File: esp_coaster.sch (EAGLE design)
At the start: 21 parts, among them IC1 ESP-12E/F, U1 MC34063AP

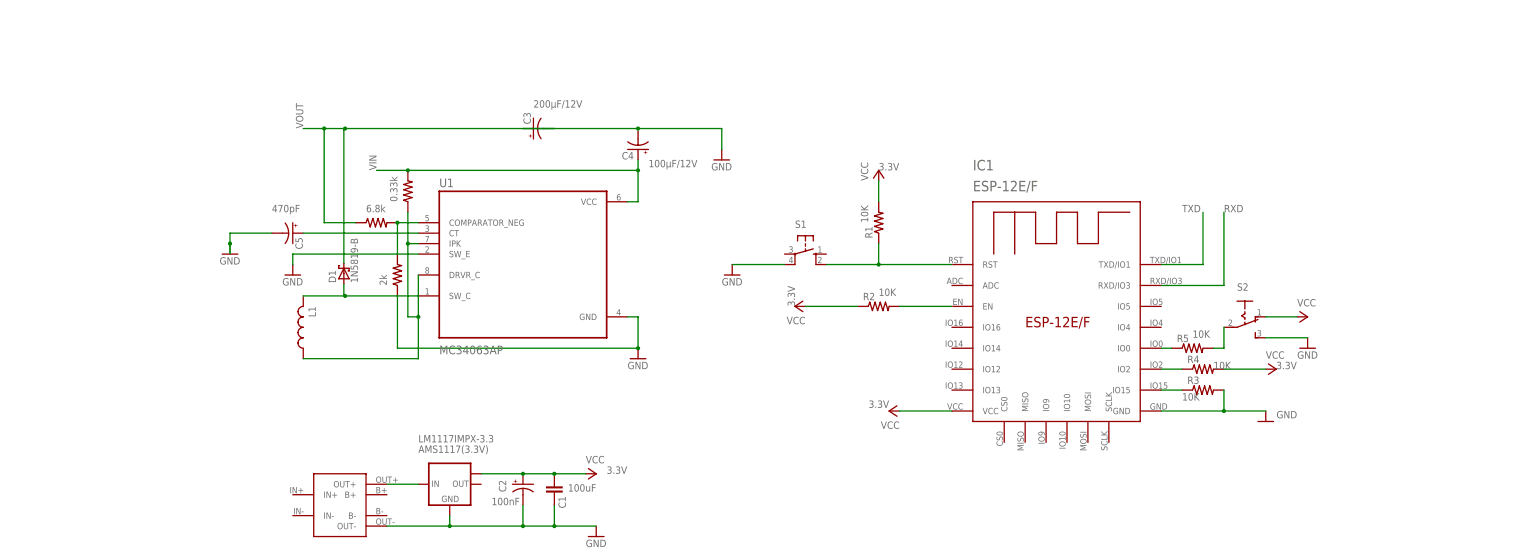
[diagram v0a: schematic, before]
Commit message: add leds
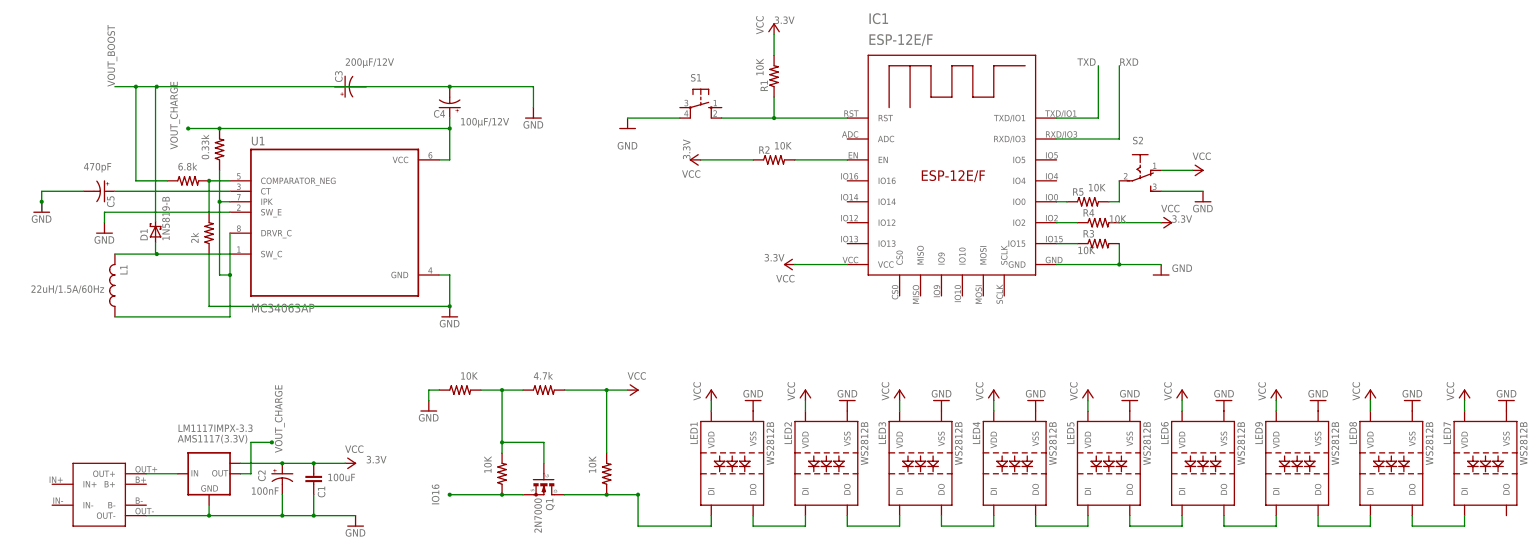
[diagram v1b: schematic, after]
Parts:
- added LED1, LED2, LED3, LED4, LED5, LED6, LED7, LED8, LED9: WS2812B, WS2812:WS2812B
- added Q1: 2N7000, 2N7000:2N7000
- added R10, R11, R12, R9: (no value), rcl:R-US_M2309
- L1: INDUCTOR (none) -> 22uH/1.5A/60Hz
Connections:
- net VOUT renamed VOUT_BOOST
- removed net VIN: C4.+, R8.2, U1.VCC
- new net IO16: Q1.S, R12.1
- new net N$12: LED1.DO, LED2.DI
- new net N$13: LED1.DI, Q1.D, R9.1
- new net N$14: Q1.G, R10.1, R11.2, R12.2
- new net N$15: LED2.DO, LED3.DI
- new net N$16: LED3.DO, LED4.DI
- new net N$17: LED4.DO, LED5.DI
- new net N$18: LED5.DO, LED6.DI
- new net N$19: LED6.DO, LED9.DI
- new net N$20: LED8.DI, LED9.DO
- new net N$21: LED7.DI, LED8.DO
- new net VOUT_CHARGE: AMS1117(3.3V).OUT, C4.+, R8.2, U1.VCC
- net GND: now also LED1.VSS, LED2.VSS, LED3.VSS, LED4.VSS, LED5.VSS, LED6.VSS, LED7.VSS, LED8.VSS, LED9.VSS, R11.1
- net VCC: now also LED1.VDD, LED2.VDD, LED3.VDD, LED4.VDD, LED5.VDD, LED6.VDD, LED7.VDD, LED8.VDD, LED9.VDD, R10.2, R9.2
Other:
- moved on the sheet: AMS1117(3.3V), C1, C2, C3, C4, C5, D1, IC1, L1, R1, R2, R3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
